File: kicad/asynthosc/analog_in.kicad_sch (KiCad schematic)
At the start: 9 parts, among them J6 AudioJack3, U8 MCP6004, U9 MCP6004

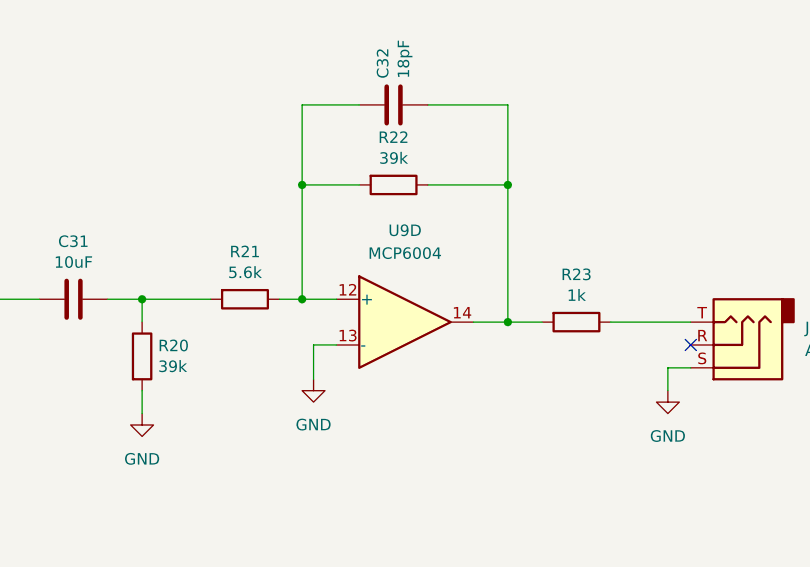
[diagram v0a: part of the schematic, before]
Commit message: pcb: place and change some components for easier routing
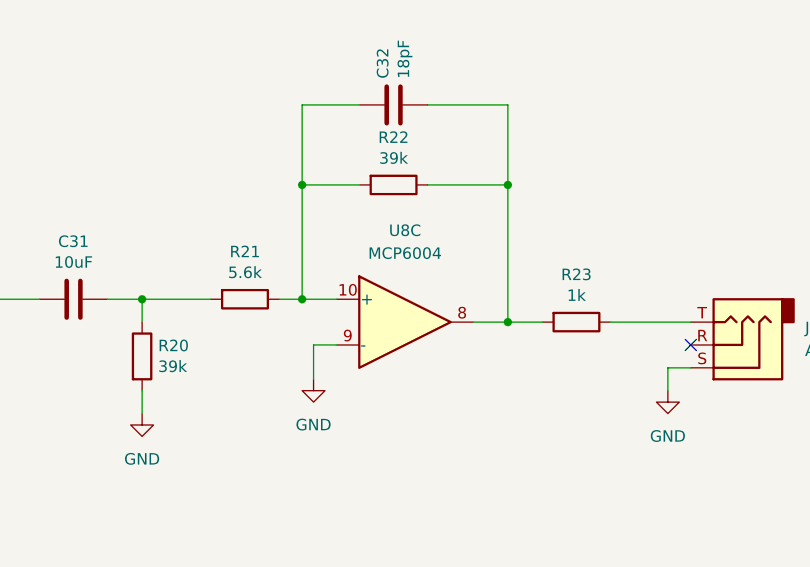
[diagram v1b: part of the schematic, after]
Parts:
- renumbered U9 to U8
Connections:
- net GND: now also U8.9 (-); no longer U8.13 (-)
- net at C32.1, R21.1, R22.2: now also U8.10 (+); no longer U8.12 (+)
- net at C32.2, R22.1, R23.2: now also U8.8; no longer U8.14
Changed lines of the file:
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@@
 		(dnp no)
 		(fields_autoplaced yes)
-		(property "Reference" "#PWR062"
+		(property "Reference" "#PWR063"
 			(at 220.98 78.74 0)
 			(effects
@@
 			(project "asynthosc"
 				(path "/d73e377a-a016-415f-8824-91cc6e4907b9/5f8430bb-1923-4d76-b418-f207310879ec"
-					(reference "#PWR062")
+					(reference "#PWR063")
 					(unit 1)
 				)
@@
 		(dnp no)
 		(fields_autoplaced yes)
-		(property "Reference" "#PWR058"
+		(property "Reference" "#PWR059"
 			(at 52.07 146.05 0)
 			(effects
@@
 			(project "asynthosc"
 				(path "/d73e377a-a016-415f-8824-91cc6e4907b9/5f8430bb-1923-4d76-b418-f207310879ec"
-					(reference "#PWR058")
+					(reference "#PWR059")
 					(unit 1)
 				)
@@
 		(dnp no)
 		(fields_autoplaced yes)
-		(property "Reference" "#PWR060"
+		(property "Reference" "#PWR061"
 			(at 162.56 81.28 0)
 			(effects
@@
 			(project "asynthosc"
 				(path "/d73e377a-a016-415f-8824-91cc6e4907b9/5f8430bb-1923-4d76-b418-f207310879ec"
-					(reference "#PWR060")
+					(reference "#PWR061")
 					(unit 1)
 				)
@@
 		(dnp no)
 		(fields_autoplaced yes)
-		(property "Reference" "#PWR056"
+		(property "Reference" "#PWR057"
 			(at 29.21 146.05 0)
 			(effects
@@
 			(project "asynthosc"
 				(path "/d73e377a-a016-415f-8824-91cc6e4907b9/5f8430bb-1923-4d76-b418-f207310879ec"
-					(reference "#PWR056")
+					(reference "#PWR057")
 					(unit 1)
 				)
@@
 		(dnp no)
 		(fields_autoplaced yes)
-		(property "Reference" "#PWR061"
+		(property "Reference" "#PWR062"
 			(at 181.61 77.47 0)
 			(effects
@@
 			(project "asynthosc"
 				(path "/d73e377a-a016-415f-8824-91cc6e4907b9/5f8430bb-1923-4d76-b418-f207310879ec"
-					(reference "#PWR061")
+					(reference "#PWR062")
 					(unit 1)
 				)
@@
 		(dnp no)
 		(fields_autoplaced yes)
-		(property "Reference" "#PWR057"
+		(property "Reference" "#PWR058"
 			(at 29.21 163.83 0)
 			(effects
@@
 			(project "asynthosc"
 				(path "/d73e377a-a016-415f-8824-91cc6e4907b9/5f8430bb-1923-4d76-b418-f207310879ec"
-					(reference "#PWR057")
+					(reference "#PWR058")
 					(unit 1)
 				)
@@
 		(dnp no)
 		(fields_autoplaced yes)
-		(property "Reference" "#PWR059"
+		(property "Reference" "#PWR060"
 			(at 52.07 163.83 0)
 			(effects
@@
 			(project ""
 				(path "/d73e377a-a016-415f-8824-91cc6e4907b9/5f8430bb-1923-4d76-b418-f207310879ec"
-					(reference "#PWR059")
+					(reference "#PWR060")
 					(unit 1)
 				)
@@
 		(lib_id "Amplifier_Operational:MCP6004")
 		(at 191.77 64.77 0)
-		(unit 4)
+		(unit 3)
 		(exclude_from_sim no)
 		(in_bom yes)
@@
 		(dnp no)
 		(fields_autoplaced yes)
-		(property "Reference" "U9"
+		(property "Reference" "U8"
 			(at 191.77 54.61 0)
 			(effects
@@
 			(project "asynthosc"
 				(path "/d73e377a-a016-415f-8824-91cc6e4907b9/5f8430bb-1923-4d76-b418-f207310879ec"
-					(reference "U9")
-					(unit 4)
-				)
-			)
+					(reference "U8")
+					(unit 3)
+				)
+			)

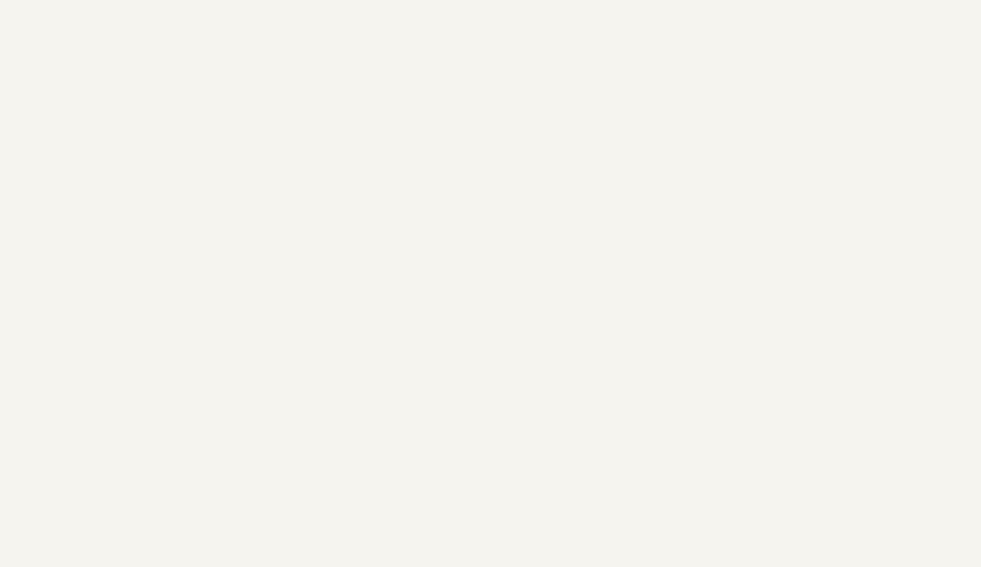
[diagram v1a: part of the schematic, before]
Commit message: sch: pcb: fix pin errors
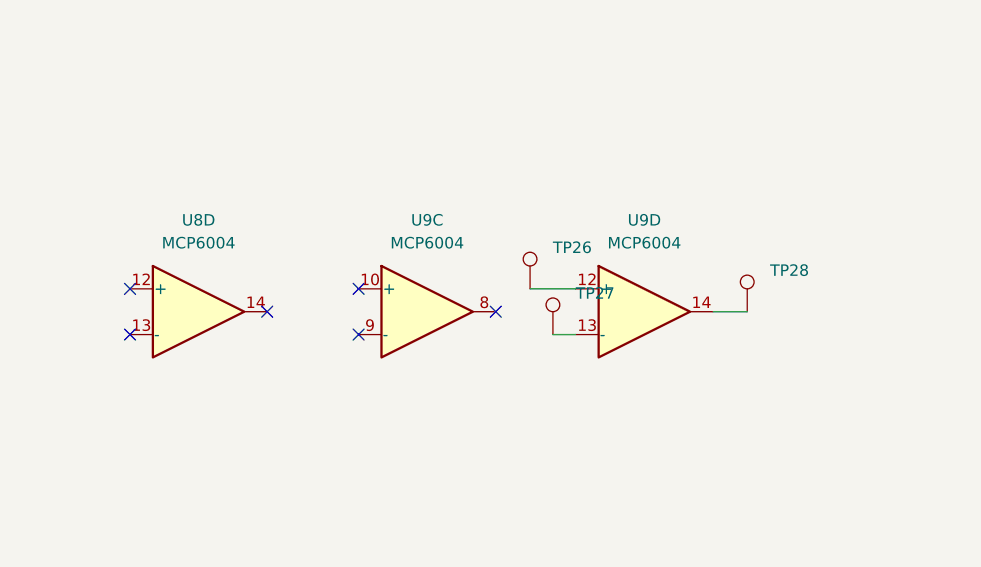
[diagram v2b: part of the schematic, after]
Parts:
- added TP26, TP27, TP28: TestPoint, TestPoint:TestPoint_Pad_D1.0mm, symbol Connector:TestPoint
- added unit 4 of U8
- added unit 3 of U9
- added unit 4 of U9
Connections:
- new net: TP27.1, U9.13 (-)
- new net: TP26.1, U9.12 (+)
- new net: TP28.1, U9.14
- no-connect marks 1 -> 7

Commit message: bom: update mfr, serials and lcsc fields
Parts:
- J6: LCSC (none) -> C381132
- U8, U9: LCSC (none) -> C627416
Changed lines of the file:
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@@
 			)
 		)
-		(property "LCSC" ""
+		(property "LCSC" "C627416"
 			(at 31.75 149.86 0)
 			(effects
@@
 			)
 		)
-		(property "LCSC" ""
+		(property "LCSC" "C627416"
 			(at 67.31 104.14 0)
 			(effects
@@
 			)
 		)
-		(property "LCSC" ""
+		(property "LCSC" "C381132"
 			(at 228.6 67.31 0)
 			(effects
@@
 			)
 		)
-		(property "LCSC" ""
+		(property "LCSC" "C627416"
 			(at 41.91 104.14 0)
 			(effects
@@
 			)
 		)
-		(property "LCSC" ""
+		(property "LCSC" "C627416"
 			(at 54.61 149.86 0)
 			(effects
@@
 			)
 		)
-		(property "LCSC" ""
+		(property "LCSC" "C627416"
 			(at 91.44 104.14 0)
 			(effects
@@
 			)
 		)
-		(property "LCSC" ""
+		(property "LCSC" "C627416"
 			(at 191.77 64.77 0)
 			(effects

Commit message: bom: add jlcpcb field with simplified footprint
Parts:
- C31: JLC (none) -> 0805
- C32: JLC (none) -> 0603
- R20, R21, R22, R23: JLC (none) -> 0402
- U8, U9: JLC (none) -> TSSOP-14
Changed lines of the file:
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@@
+			)
+		)
+		(property "JLC" "0805"
+			(at 154.94 62.23 0)
+			(effects
+				(font
+					(size 1.27 1.27)
+				)
+				(hide yes)
 			)
 		)
@@
 			)
 		)
+		(property "JLC" ""
+			(at 81.28 106.68 0)
+			(effects
+				(font
+					(size 1.27 1.27)
+				)
+				(hide yes)
+			)
+		)
 		(pin "1"
 		)
@@
 			)
 		)
+		(property "JLC" "0402"
+			(at 162.56 68.58 0)
+			(effects
+				(font
+					(size 1.27 1.27)
+				)
+				(hide yes)
+			)
+		)
 		(pin "1"
 		)
@@
 			)
 		)
+		(property "JLC" "TSSOP-14"
+			(at 31.75 149.86 0)
+			(effects
+				(font
+					(size 1.27 1.27)
+				)
+				(hide yes)
+			)
+		)
 		(pin "1"
 		)
@@
 			)
 		)
+		(property "JLC" "TSSOP-14"
+			(at 67.31 104.14 0)
+			(effects
+				(font
+					(size 1.27 1.27)
+				)
+				(hide yes)
+			)
+		)
 		(pin "1"
 		)
@@
 			)
 		)
+		(property "JLC" "0402"
+			(at 173.99 62.23 0)
+			(effects
+				(font
+					(size 1.27 1.27)
+				)
+				(hide yes)
+			)
+		)
 		(pin "1"
 		)
@@
 		)
 		(property "RefNum" "_generic_"
+			(at 190.5 49.53 0)
+			(effects
+				(font
+					(size 1.27 1.27)
+				)
+				(hide yes)
+			)
+		)
+		(property "JLC" "0402"
 			(at 190.5 49.53 0)
 			(effects
@@
 			)
 		)
+		(property "JLC" ""
+			(at 228.6 67.31 0)
+			(effects
+				(font
+					(size 1.27 1.27)
+				)
+				(hide yes)
+			)
+		)
 		(pin "S"
 		)
@@
 			)
 		)
+		(property "JLC" "TSSOP-14"
+			(at 41.91 104.14 0)
+			(effects
+				(font
+					(size 1.27 1.27)
+				)
+				(hide yes)
+			)
+		)
 		(pin "1"
 		)
@@
 			)
 		)
+		(property "JLC" ""
+			(at 78.74 101.6 0)
+			(effects
+				(font
+					(size 1.27 1.27)
+				)
+				(hide yes)
+			)
+		)
 		(pin "1"
 		)
@@
 		)
 		(property "RefNum" "_generic_"
+			(at 210.82 64.77 0)
+			(effects
+				(font
+					(size 1.27 1.27)
+				)
+				(hide yes)
+			)
+		)
+		(property "JLC" "0402"
 			(at 210.82 64.77 0)
 			(effects
@@
 			)
 		)
+		(property "JLC" "TSSOP-14"
+			(at 54.61 149.86 0)
+			(effects
+				(font
+					(size 1.27 1.27)
+				)
+				(hide yes)
+			)
+		)
 		(pin "1"
 		)
@@
 		)
 		(property "RefNum" "_generic_"
+			(at 190.5 40.64 0)
+			(effects
+				(font
+					(size 1.27 1.27)
+				)
+				(hide yes)
+			)
+		)
+		(property "JLC" "0603"
 			(at 190.5 40.64 0)
 			(effects
@@
 			)
 		)
+		(property "JLC" "TSSOP-14"
+			(at 91.44 104.14 0)
+			(effects
+				(font
+					(size 1.27 1.27)
+				)
+				(hide yes)
+			)
+		)
 		(pin "1"
 		)
@@
 			)
 		)
+		(property "JLC" "TSSOP-14"
+			(at 191.77 64.77 0)
+			(effects
+				(font
+					(size 1.27 1.27)
+				)
+				(hide yes)
+			)
+		)
 		(pin "1"
 		)
@@
 			(at 102.87 104.14 0)
 			(effects
+				(font
+					(size 1.27 1.27)
+				)
+				(hide yes)
+			)
+		)
+		(property "JLC" ""
+			(at 102.87 104.14 0)
+			(effects

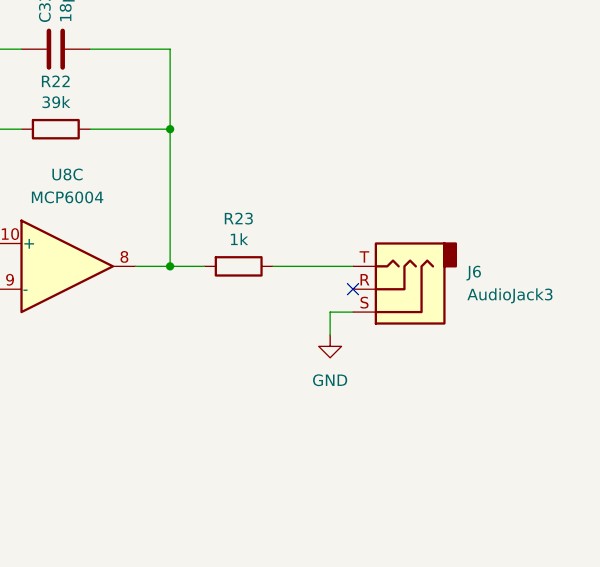
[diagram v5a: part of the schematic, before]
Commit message: bom: dnp for all manually equiped components
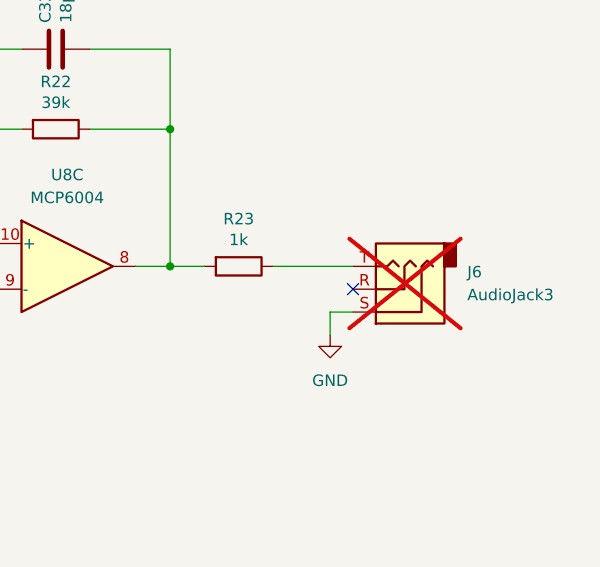
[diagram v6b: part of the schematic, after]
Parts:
- J6: now not fitted
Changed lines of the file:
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@@
 		(in_bom yes)
 		(on_board yes)
-		(dnp no)
+		(dnp yes)
 		(fields_autoplaced yes)
 		(property "Reference" "J6"

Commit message: bom: adding jlc ref to generic
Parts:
- C31: LCSC (none) -> C15850
- C32: LCSC (none) -> C1647
- R20, R22: LCSC (none) -> C25783
- R21: LCSC (none) -> C25908
- R23: LCSC (none) -> C11702
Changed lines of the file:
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@@
 			)
 		)
-		(property "LCSC" ""
+		(property "LCSC" "C15850"
 			(at 154.94 62.23 0)
 			(effects
@@
 			)
 		)
-		(property "LCSC" ""
+		(property "LCSC" "C25783"
 			(at 162.56 68.58 0)
 			(effects
@@
 			)
 		)
-		(property "LCSC" ""
+		(property "LCSC" " C25908"
 			(at 173.99 62.23 0)
 			(effects
@@
 			)
 		)
-		(property "LCSC" ""
+		(property "LCSC" "C25783"
 			(at 190.5 49.53 0)
 			(effects
@@
 			)
 		)
-		(property "LCSC" ""
+		(property "LCSC" "C11702"
 			(at 210.82 64.77 0)
 			(effects
@@
 			)
 		)
-		(property "LCSC" ""
+		(property "LCSC" "C1647"
 			(at 190.5 40.64 0)
 			(effects
